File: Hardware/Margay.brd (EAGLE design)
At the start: 50.2 x 30.4 mm, 61 parts, among them IC1 ATMEGA644M, J1 CONN_4SCREW_2.54, J2 CONN_6, Q1 MOSFET_PCH-IRLML2244, Q2 MOSFET-NCH-DMG3404L, Q5 MOSFET_PCH-IRLML2244, U2 FT231X-Q

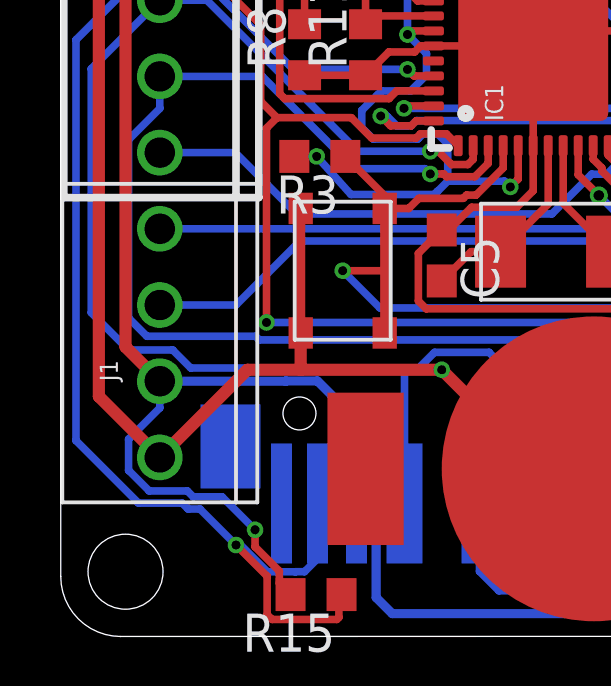
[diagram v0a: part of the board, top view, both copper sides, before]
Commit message: Added software folder to repo
Software folder containing hardware test script as well as logger code which supports the TP-Downhole
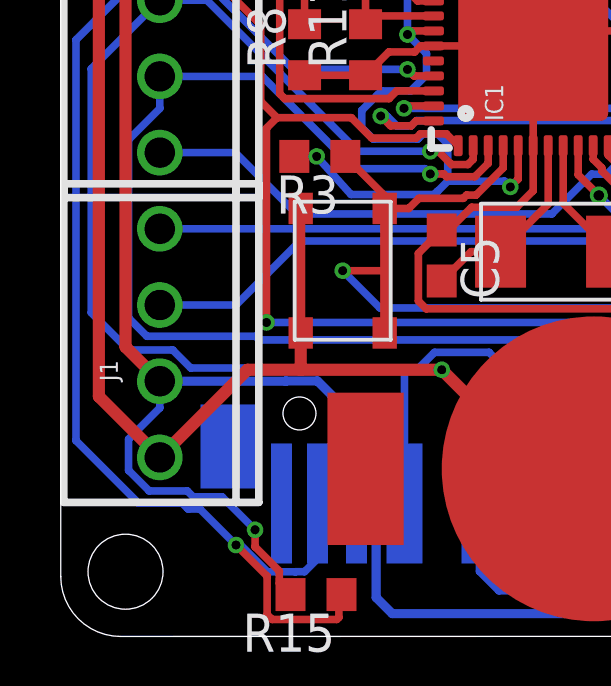
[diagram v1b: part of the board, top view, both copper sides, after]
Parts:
- J2: value CONN_6 -> CONN_6SCREW_2.54
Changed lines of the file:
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@@
 <attribute name="NAME" x="32.639" y="1.016" size="1.27" layer="25" rot="R90"/>
 </element>
-<element name="J1" library="bschulz" package="1X04" value="CONN_4SCREW_2.54" x="3.302" y="9.779" rot="R90"/>
-<element name="J2" library="bschulz" package="1X06_SCREW" value="CONN_6" x="3.302" y="22.479" rot="R270"/>
-<element name="J3" library="bschulz" package="1X02_2.54_SCREWTERM" value="" x="46.355" y="16.129" rot="R270"/>
-<element name="J4" library="bschulz" package="1X02_2.54_SCREWTERM" value="" x="46.355" y="11.049" rot="R270"/>
-<element name="J5" library="bschulz" package="1X02_2.54_SCREWTERM" value="" x="46.355" y="5.969" rot="R270"/>
+<element name="J1" library="bschulz" package="1X04" value="CONN_4SCREW_2.54" x="3.302" y="9.779" rot="R90">
+<attribute name="DIGIKEY" value="ED10563-ND" x="3.302" y="9.779" size="1.778" layer="27" rot="R90" display="off"/>
+<attribute name="MF" value="OnShore" x="3.302" y="9.779" size="1.778" layer="27" rot="R90" display="off"/>
+<attribute name="MPN" value="OSTVN04A150" x="3.302" y="9.779" size="1.778" layer="27" rot="R90" display="off"/>
+</element>
+<element name="J2" library="bschulz" package="1X06_SCREW" value="CONN_6SCREW_2.54" x="3.302" y="22.479" rot="R270">
+<attribute name="DIGIKEY" value="ED10565-ND" x="3.302" y="22.479" size="1.778" layer="27" rot="R270" display="off"/>
+<attribute name="MF" value="OnShore" x="3.302" y="22.479" size="1.778" layer="27" rot="R270" display="off"/>
+<attribute name="MPN" value="OSTVN06A150" x="3.302" y="22.479" size="1.778" layer="27" rot="R270" display="off"/>
+</element>
+<element name="J3" library="bschulz" package="1X02_2.54_SCREWTERM" value="" x="46.355" y="16.129" rot="R270">
+<attribute name="DIGIKEY" value="ED10561-ND" x="46.355" y="16.129" size="1.778" layer="27" rot="R270" display="off"/>
+<attribute name="MF" value="OnShore" x="46.355" y="16.129" size="1.778" layer="27" rot="R270" display="off"/>
+<attribute name="MPN" value="OSTVN02A150" x="46.355" y="16.129" size="1.778" layer="27" rot="R270" display="off"/>
+</element>
+<element name="J4" library="bschulz" package="1X02_2.54_SCREWTERM" value="" x="46.355" y="11.049" rot="R270">
+<attribute name="DIGIKEY" value="ED10561-ND" x="46.355" y="11.049" size="1.778" layer="27" rot="R270" display="off"/>
+<attribute name="MF" value="OnShore" x="46.355" y="11.049" size="1.778" layer="27" rot="R270" display="off"/>
+<attribute name="MPN" value="OSTVN02A150" x="46.355" y="11.049" size="1.778" layer="27" rot="R270" display="off"/>
+</element>
+<element name="J5" library="bschulz" package="1X02_2.54_SCREWTERM" value="" x="46.355" y="5.969" rot="R270">
+<attribute name="DIGIKEY" value="ED10561-ND" x="46.355" y="5.969" size="1.778" layer="27" rot="R270" display="off"/>
+<attribute name="MF" value="OnShore" x="46.355" y="5.969" size="1.778" layer="27" rot="R270" display="off"/>
+<attribute name="MPN" value="OSTVN02A150" x="46.355" y="5.969" size="1.778" layer="27" rot="R270" display="off"/>
+</element>
 <element name="JP1" library="SparkFun-Jumpers" library_urn="urn:adsk.eagle:library:528" package="SMT-JUMPER_3_1-NC_PASTE_SILK" package3d_urn="urn:adsk.eagle:package:39293/1" value="JUMPER-SMT_3_1-NC_PASTE_SILK" x="43.561" y="6.096" rot="MR270"/>
 <element name="JP2" library="SparkFun-Jumpers" library_urn="urn:adsk.eagle:library:528" package="SMT-JUMPER_2_NC_PASTE_SILK" package3d_urn="urn:adsk.eagle:package:39282/1" value="JUMPER-SMT_2_NC_PASTE_SILK" x="38.481" y="11.938"/>

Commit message: Added revision notes to board
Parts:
- R11, R9: value (none) -> 1.62M
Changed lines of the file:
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@@
 <attribute name="VALUE_PART" value="330" x="21.336" y="29.083" size="1.778" layer="27" display="off"/>
 </element>
-<element name="R11" library="bschulz" package="R0603" value="" x="10.16" y="19.558" rot="R90">
+<element name="R11" library="bschulz" package="R0603" value="1.62M" x="10.16" y="19.558" rot="R90">
 <attribute name="DIGIKEY" value="" x="10.16" y="19.558" size="1.778" layer="27" rot="R90" display="off"/>
 <attribute name="MF" value="" x="10.16" y="19.558" size="1.778" layer="27" rot="R90" display="off"/>
@@
 <attribute name="VALUE_PART" value="" x="8.128" y="19.558" size="1.778" layer="27" rot="R90" display="off"/>
 </element>
-<element name="R9" library="bschulz" package="R0603" value="" x="10.16" y="22.733" rot="R90">
+<element name="R9" library="bschulz" package="R0603" value="1.62M" x="10.16" y="22.733" rot="R90">
 <attribute name="DIGIKEY" value="" x="10.16" y="22.733" size="1.778" layer="27" rot="R90" display="off"/>
 <attribute name="MF" value="" x="10.16" y="22.733" size="1.778" layer="27" rot="R90" display="off"/>

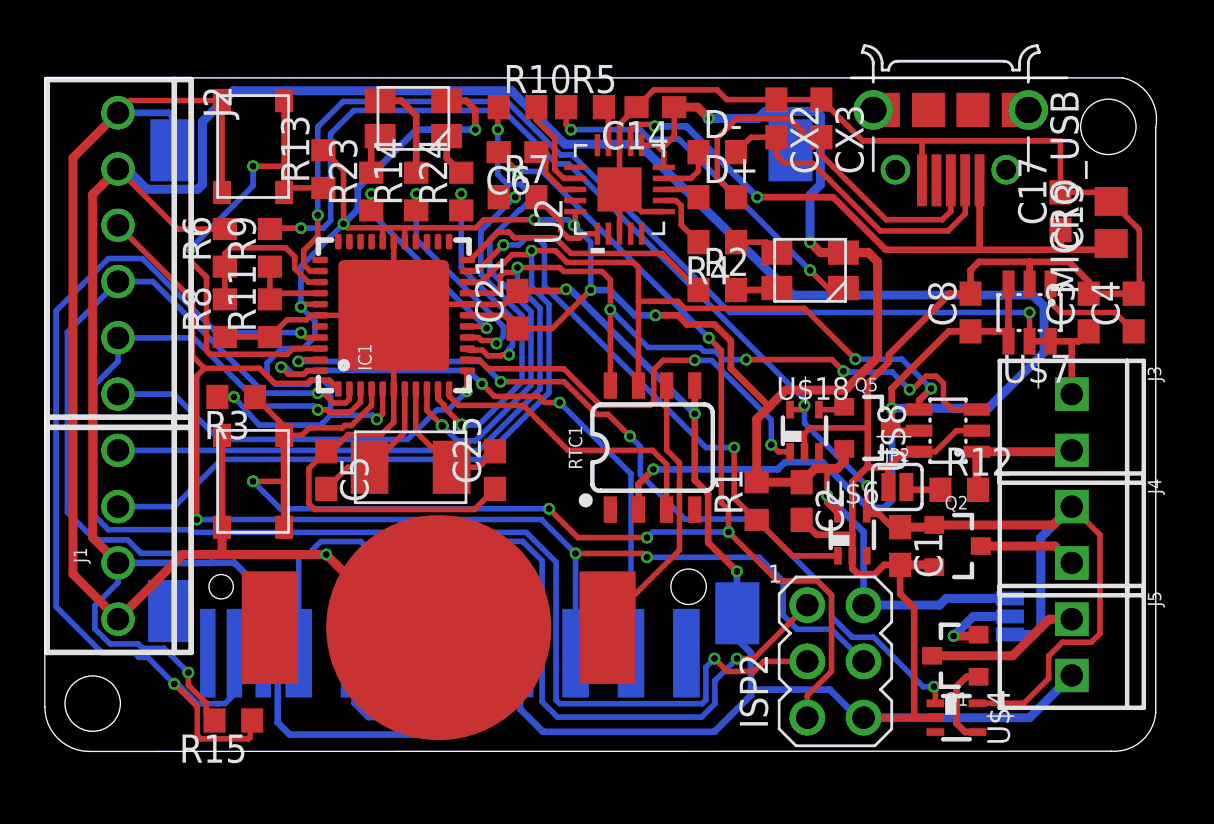
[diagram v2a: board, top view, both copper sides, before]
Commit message: Margay 1.0 initial layout
Initial layout of the version 1.0 , solder jumpers currently not added, along with battery connector, may intoduce back later, needs cleanup and DRC
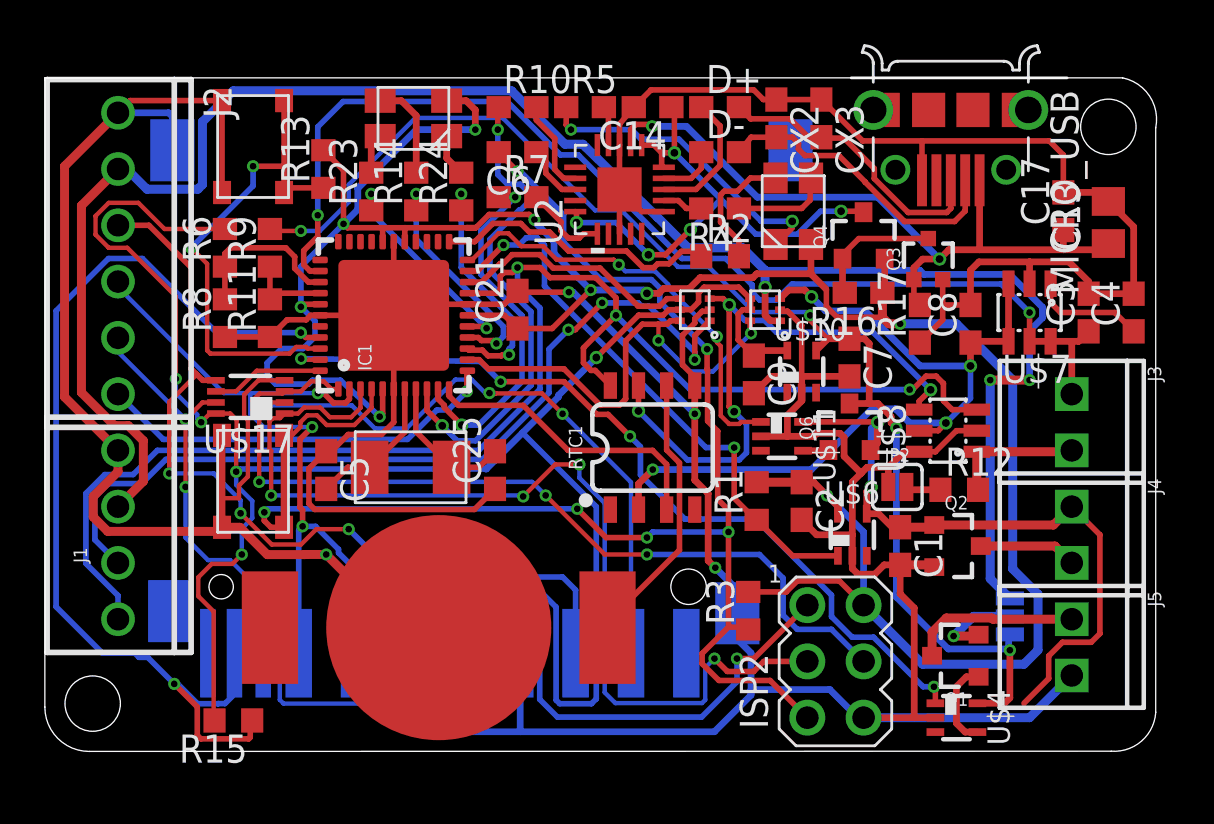
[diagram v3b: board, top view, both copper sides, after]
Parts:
- removed Q5: MOSFET_PCH-IRLML2244, bschulz:SOT23-3
- removed U$18: MIC842, bschulz:DCK_R-PDSO-G5
- added C7: 0.1uF, bschulz_passives:C0603
- added C9: 0.47uF, bschulz_passives:C0603
- added Q3: 2N7002, bschulz:SOT323
- added Q4, Q6: FDN360P, bschulz:SOT23-3
- added R16: 180k, bschulz_passives:R0603
- added R17: 10k, bschulz_passives:R0603
- added U$10: TPS79733, bschulz:DCK_R-PDSO-G5
- added U$11: MIC842H, bschulz:DCK_R-PDSO-G5
- added U$12, U$13: SN74LVC1G3157DRL, bschulz:DRL_R-PDSO-N6
- added U$17: SN74AUP3G34DCU, bschulz:DCU_(R-PDSO-G8)
- BT1: device bschulz:AWICKERT_LINX_BAT-HLD-012-SMT -> bschulz:LINX_BAT-HLD-012-SMT
- D+, D-, R10, R4, R5, R7: device bschulz:R0603 -> bschulz_passives:R0603
- J1: value CONN_4SCREW_2.54 -> CONN_42.54_SCREW; device bschulz:1X04 -> bschulz:1X04_SCREW
- Q1: value MOSFET_PCH-IRLML2244 -> FDN360P
- Q2: value MOSFET-NCH-DMG3404L -> DMG3404
- U$4: value MIC842 -> MIC842H
- moved R3 25.0 mm to (31.8, 6.35), turned to 90 degrees
- moved D+ 4.07 mm to (30.5, 29.1)
- moved U$16 2.77 mm to (33.8, 24.4), turned to 90 degrees
- moved R2 1.53 mm to (30.5, 22.4)
- moved R4 1.53 mm to (30.5, 24.5)
- moved C8 0.51 mm to (41.8, 19.3)
- moved C13 0.13 mm to (48.0, 23.9)
- moved C14 0.13 mm to (27.4, 29.1)
- moved D- 0.13 mm to (30.5, 27.1)
- moved C17 0.13 mm to (46.0, 24.4)
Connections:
- removed net 3.3V_EXT_CTRL: IC1.13, U$18.1
- removed net EXT_3.3V: C8.1, J1.2, J2.2, Q5.3, R15.2, R6.2, RTC1.2, U$3.4, U$7.3, U$7.4, U$8.5
- removed net N$7: Q5.1, U$18.4
- new net 3V3_AUX: C9.1, R15.2, R6.2, U$10.5, U$12.4, U$12.5, U$13.5, U$17.8, U$3.4
- new net 3V3_AUX_CTRL: IC1.13, U$12.6, U$13.6
- new net 3V3_EXT: J1.3, J2.2, JP1.1, U$12.1
- new net 3V3_FTDI: C14.1, Q4.3, U2.10, U2.11, U2.20
- new net 3V3_OB: C8.1, RTC1.2, U$12.3, U$7.3, U$7.4, U$8.5
- new net MOSI_BUF: J2.3, U$17.5, U$3.2
- new net N$4: Q6.1, U$11.4
- new net N$6: Q3.3, Q4.1, R16.2
- new net SCK_BUF: J2.5, U$17.7, U$3.5
- new net SDA_EXT: J1.2, U$13.1
- new net SDA_OB: RTC1.7, U$13.3, U$8.4
- new net SD_CS_BUF: U$17.2, U$3.1
- new net VBAT_SW: C7.1, JP1.3, Q6.3, R9.2, U$10.4, U$4.5
- new net VBAT_SW_CTRL: IC1.22, U$11.1
- net 3V3: now also Q4.2, R16.1; no longer C14.1, JP1.1, Q5.2, U2.10, U2.11, U2.20
- net GND: now also C7.2, C9.2, J1.4, Q3.2, R17.1, U$10.2, U$11.2, U$12.2, U$13.2, U$17.4; no longer J1.1, U$18.2
- net MOSI: now also U$17.3; no longer J2.3, U$3.2
- net N$1: now also IC1.23; no longer IC1.22
- net SCK: now also U$17.1; no longer J2.5, U$3.5
- net SCL: now also J1.1; no longer J1.4
- net SDA: now also U$13.4; no longer J1.3, RTC1.7, U$8.4
- net SD_CS: now also U$17.6; no longer U$3.1
- net VBAT+: now also Q6.2, U$11.5; no longer JP1.3, R9.2, U$18.5, U$4.5
- net VUSB: now also Q3.1, R17.2
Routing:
- net EXT_3.3V: track 151.1 -> 0.00 mm, vias 3 -> 0
- net 3V3_AUX: track 0.00 -> 94.5 mm, vias 0 -> 5
- net 3V3_EXT: track 0.00 -> 85.9 mm, vias 0 -> 3
- net VBAT_SW: track 0.00 -> 59.0 mm, vias 0 -> 4
- net SDA: track 58.3 -> 11.2 mm, vias 3 -> 0
- net VBAT+: track 72.7 -> 30.9 mm, vias 3 -> 2
- net MOSI_BUF: track 0.00 -> 39.3 mm, vias 0 -> 3
- net SDA_EXT: track 0.00 -> 38.6 mm, vias 0 -> 3
- net 3V3_OB: track 0.00 -> 36.8 mm, vias 0 -> 4
- net SCK_BUF: track 0.00 -> 29.8 mm, vias 0 -> 2
- net SD_CS_BUF: track 0.00 -> 28.5 mm, vias 0 -> 3
- net SDA_OB: track 0.00 -> 26.9 mm, vias 0 -> 4
- net 3V3_FTDI: track 0.00 -> 23.6 mm, vias 0 -> 5
- net SD_CS: track 28.0 -> 5.09 mm, vias 3 -> 0
- net SCK: track 68.5 -> 45.7 mm, vias 2 -> 4
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
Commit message: Cleaned up board, removed power switch
Cleaned up the routing, removed the switched power
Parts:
- removed U$12: SN74LVC1G3157DRL, bschulz:DRL_R-PDSO-N6
- added JP3: JUMPER-SMT_2_NO_SILK, SparkFun-Jumpers:SMT-JUMPER_2_NO_SILK
- moved U$2 4.73 mm to (40.5, 12.4)
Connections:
- removed net 3V3_EXT: J1.3, J2.2, JP1.1, U$12.1
- removed net 3V3_OB: C8.1, RTC1.2, U$12.3, U$7.3, U$7.4, U$8.5
- net 3V3_AUX: now also C8.1, J1.3, J2.2, JP1.1, RTC1.2, U$7.3, U$7.4, U$8.5; no longer U$12.4, U$12.5
- net 3V3_AUX_CTRL: no longer U$12.6
- net GND: no longer U$12.2
- net SDA_EXT: now also JP3.2
- net SDA_OB: now also JP3.1
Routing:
- net 3V3_AUX: track 94.5 -> 216.2 mm, vias 5 -> 12
- net 3V3_EXT: track 85.9 -> 0.00 mm, vias 3 -> 0
- net 3V3_OB: track 36.8 -> 0.00 mm, vias 4 -> 0
- net 3V3_AUX_CTRL: track 20.3 -> 13.6 mm, vias 2 -> 0
- net SDA_EXT: track 38.6 -> 44.5 mm
- net GND: track 280.3 -> 276.7 mm
- net SDA_OB: track 26.9 -> 27.5 mm
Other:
- board text added: "J2"
- board text added: "Project Margay v1.0 ---------------- Developed by Northern Widget and University of Minnesota"
- board text removed: "Project Margay v0.0 ---------------- Developed by Northern Widget and University of Minnesota"

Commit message: Updated board, fixed software logging time
Cleaned up traces on board, changed battery in schematic, updated logging program to have 15 minute interval by default
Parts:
- U$1: value CRYSTAL_5X3.2_2LEAD -> CRYSTAL8MHZ5X3.2
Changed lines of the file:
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@@
 <attribute name="MPN" value="DS3231MZ+" x="27.432" y="13.716" size="1.778" layer="27" display="off"/>
 </element>
-<element name="U$1" library="bschulz" package="CRYSTAL_5X3.2_2-SMD" value="CRYSTAL_5X3.2_2LEAD" x="16.51" y="12.827" rot="R180">
-<attribute name="DIGIKEY" value="" x="16.51" y="12.827" size="1.778" layer="27" rot="R180" display="off"/>
-<attribute name="MF" value="" x="16.51" y="12.827" size="1.778" layer="27" rot="R180" display="off"/>
-<attribute name="MPN" value="" x="16.51" y="12.827" size="1.778" layer="27" rot="R180" display="off"/>
+<element name="U$1" library="bschulz" package="CRYSTAL_5X3.2_2-SMD" value="CRYSTAL8MHZ5X3.2" x="16.51" y="12.827" rot="R180">
+<attribute name="DIGIKEY" value="887-1740-1-ND" x="16.51" y="12.827" size="1.778" layer="27" rot="R180" display="off"/>
+<attribute name="MF" value="TXC" x="16.51" y="12.827" size="1.778" layer="27" rot="R180" display="off"/>
+<attribute name="MPN" value="7A-8.000MAAE-T" x="16.51" y="12.827" size="1.778" layer="27" rot="R180" display="off"/>
 </element>
 <element name="U$15" library="bschulz" package="CLVBA-FKA" value="CLVBA-FKA" x="16.637" y="28.575" rot="R180">

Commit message: Generated gerbers, ready for Mrk1
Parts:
- moved C2 1.27 mm to (34.2, 10.0)
- moved R1 1.27 mm to (32.1, 10.0)
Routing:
- net VBAT+: track 30.9 -> 19.8 mm
- net GND: track 276.7 -> 282.6 mm
- net PG: track 25.7 -> 27.0 mm
- net TX: track 16.1 -> 17.2 mm
- net VREF: track 51.2 -> 52.0 mm
- net 3V3_AUX: track 216.2 -> 216.9 mm

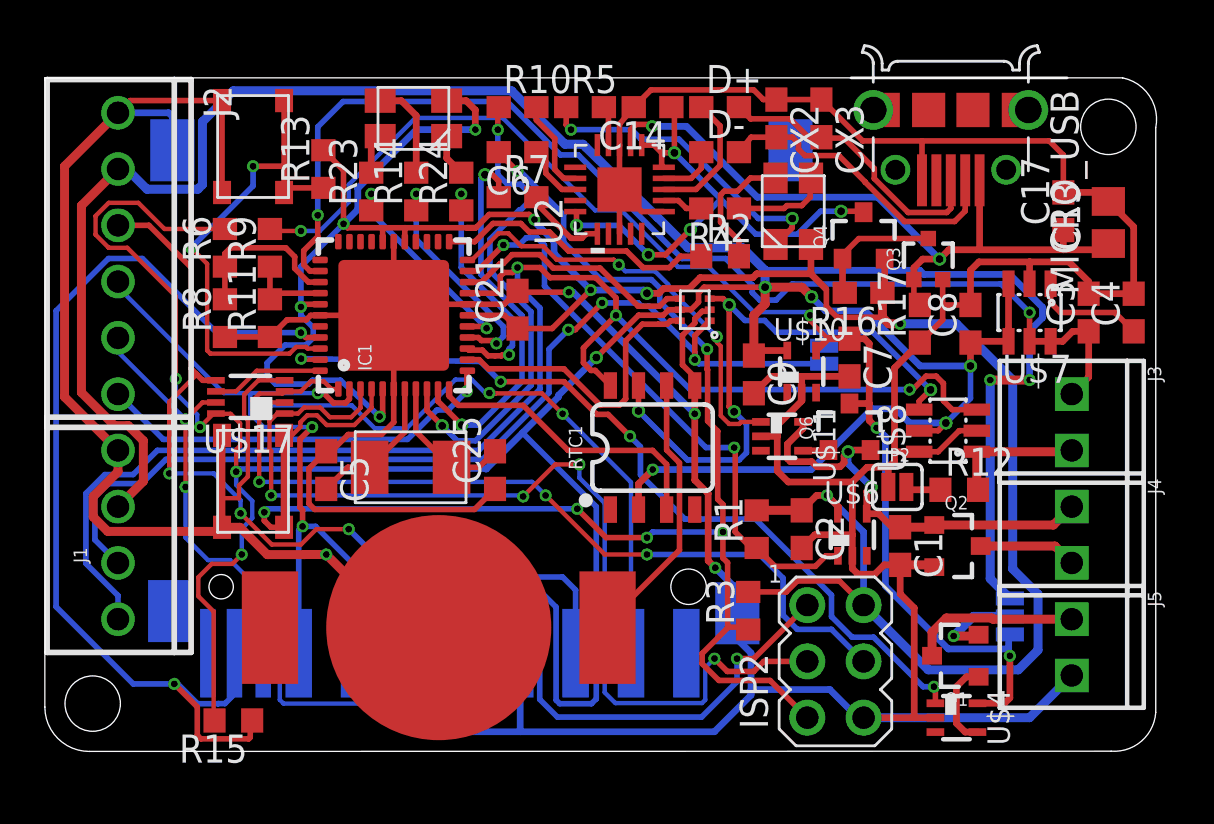
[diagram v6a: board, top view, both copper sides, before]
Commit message: Minor mod to hardware test, added BOM
Added independent BOM and did some clean up on the schematic
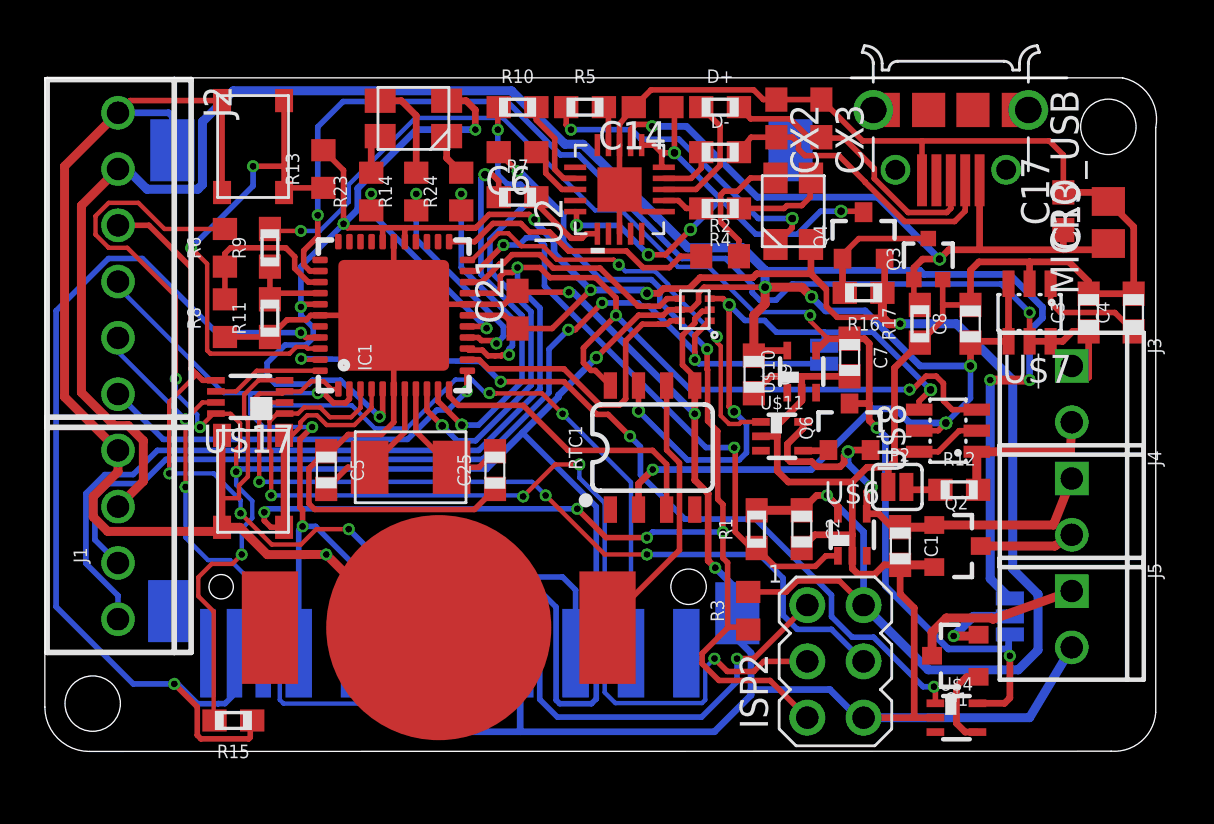
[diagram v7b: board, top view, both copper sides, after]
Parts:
- C2, C9: value 0.47uF -> 1uF
- C25, C5, C8: device bschulz:C0603 -> bschulz_passives:C0603
- R1, R11, R12, R15, R9: device bschulz:R0603 -> bschulz_passives:R0603
- R2: value 330R -> 330
- U$3: device adafruit:06132 -> bschulz:06132
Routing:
- net A0: track 6.05 -> 7.30 mm
- net VBAT+: track 19.8 -> 20.9 mm
- net GND: track 282.6 -> 283.6 mm
